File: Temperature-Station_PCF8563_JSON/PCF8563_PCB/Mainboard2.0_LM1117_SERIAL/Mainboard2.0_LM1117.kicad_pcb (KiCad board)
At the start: 2 copper layers, 32 parts, among them J1 CONN_01X03, J2 CONN_01X03, J4 SD_Card, J5 CONN_01X03, J6 CONN_01X02, J7 CONN_01X02, SW1 RESET, SW2 FLASH, U1 LM1117-3.3, U2 PCF8563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

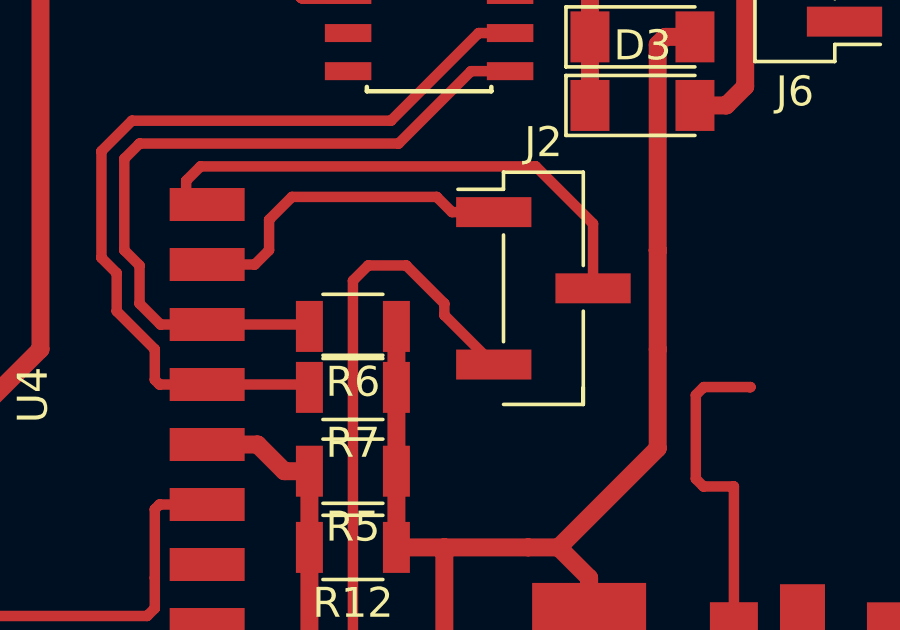
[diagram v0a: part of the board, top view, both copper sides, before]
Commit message: Updates
Updated both versions
Added online updater
Minor cosmetic changes
Saving DHCP settings restored
Added authentication (still no HTTPS/TLS/SSL tho)
Moved as many Strings as possible to Flash memory to free RAM

Czas library:
Optimized for porting between DS3231 and PCF8563 versions.
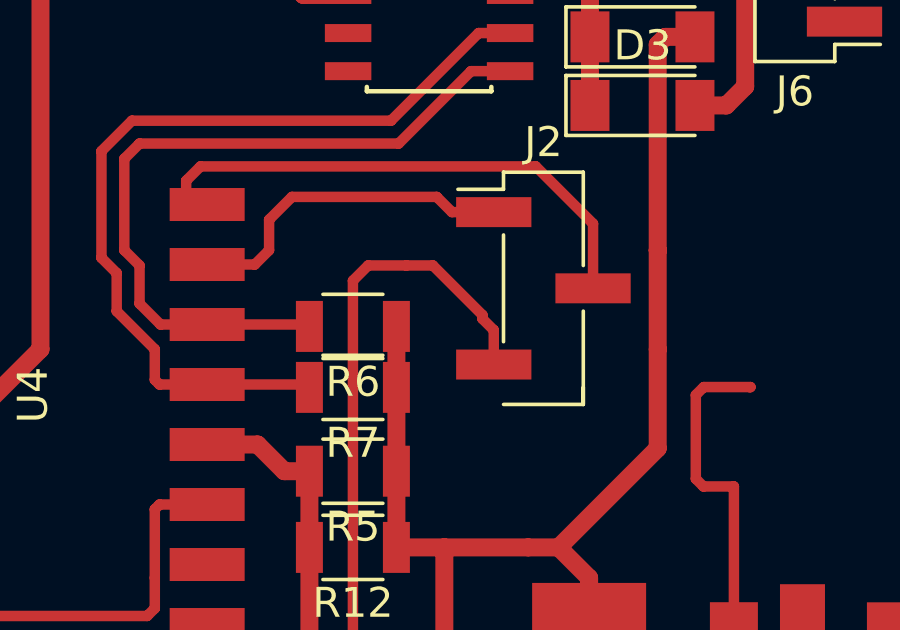
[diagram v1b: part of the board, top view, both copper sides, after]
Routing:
- net GND: track 95.2 -> 95.8 mm
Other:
- net class Default: trace_width 0.35 -> 0.25
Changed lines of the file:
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@@
-(kicad_pcb (version 4) (host pcbnew 4.0.6)
+(kicad_pcb (version 20170919) (host pcbnew "(2017-09-19 revision dddaa7e69)-makepkg")
   (general
-    (links 71)
-    (no_connects 2)
-    (area 0 0 0 0)
     (thickness 1.6)
     (drawings 0)
-    (tracks 276)
+    (tracks 278)
     (zones 0)
     (modules 32)
@@
   (layers
     (0 F.Cu signal)
-    (31 B.Cu signal hide)
-    (32 B.Adhes user hide)
-    (33 F.Adhes user hide)
-    (34 B.Paste user hide)
+    (31 B.Cu signal)
+    (32 B.Adhes user)
+    (33 F.Adhes user)
+    (34 B.Paste user)
     (35 F.Paste user)
-    (36 B.SilkS user hide)
+    (36 B.SilkS user)
     (37 F.SilkS user)
-    (38 B.Mask user hide)
+    (38 B.Mask user)
     (39 F.Mask user)
-    (40 Dwgs.User user hide)
-    (41 Cmts.User user hide)
-    (42 Eco1.User user hide)
-    (43 Eco2.User user hide)
-    (44 Edge.Cuts user hide)
-    (45 Margin user hide)
-    (46 B.CrtYd user hide)
+    (40 Dwgs.User user)
+    (41 Cmts.User user)
+    (42 Eco1.User user)
+    (43 Eco2.User user)
+    (44 Edge.Cuts user)
+    (45 Margin user)
+    (46 B.CrtYd user)
     (47 F.CrtYd user)
-    (48 B.Fab user hide)
+    (48 B.Fab user)
     (49 F.Fab user)
   )
   (setup
-    (last_trace_width 0.35)
+    (last_trace_width 0.25)
     (trace_clearance 0.2)
     (zone_clearance 0.5)
@@
     (pad_to_mask_clearance 0)
     (aux_axis_origin 0 0)
-    (visible_elements 7FFC7A21)
+    (visible_elements 7FFFFE7F)
     (pcbplotparams
       (layerselection 0x00000_00000001)
       (usegerberextensions false)
+      (usegerberattributes true)
+      (usegerberadvancedattributes true)
+      (creategerberjobfile true)
       (excludeedgelayer true)
       (linewidth 0.050000)
@@
       (hpglpenspeed 20)
       (hpglpendiameter 15)
-      (hpglpenoverlay 2)
       (psnegative false)
       (psa4output false)
@@
   (net_class Default "To jest domyślna klasa połączeń."
     (clearance 0.2)
-    (trace_width 0.35)
+    (trace_width 0.25)
     (via_dia 0.6)
     (via_drill 0.4)
@@
     (fp_line (start 3.45 4.35) (end 3.45 -4.35) (layer F.CrtYd) (width 0.05))
     (fp_line (start 3.45 -4.35) (end -3.45 -4.35) (layer F.CrtYd) (width 0.05))
-    (fp_text user %R (at -4.318 4.064 360) (layer F.Fab)
+    (fp_text user %R (at -4.318 4.064) (layer F.Fab)
       (effects (font (size 1 1) (thickness 0.15)))
     )
@@
     (fp_line (start 3.45 4.35) (end 3.45 -4.35) (layer F.CrtYd) (width 0.05))
     (fp_line (start 3.45 -4.35) (end -3.45 -4.35) (layer F.CrtYd) (width 0.05))
-    (fp_text user %R (at 0 4.572 360) (layer F.Fab)
+    (fp_text user %R (at 0 4.572) (layer F.Fab)
       (effects (font (size 1 1) (thickness 0.15)))
     )
@@
   )
   (segment (start 95.01 95.098) (end 97.384 95.098) (width 0.6) (layer F.Cu) (net 1))
+  (segment (start 95.366 94.742) (end 95.01 95.098) (width 0.6) (layer F.Cu) (net 1))
+  (segment (start 97.384 95.098) (end 97.536 94.946) (width 0.6) (layer F.Cu) (net 1))
   (segment (start 97.536 94.946) (end 97.536 93.44) (width 0.6) (layer F.Cu) (net 1))
-  (segment (start 97.384 95.098) (end 97.536 94.946) (width 0.6) (layer F.Cu) (net 1))
   (segment (start 97.536 93.44) (end 99.822 93.44) (width 0.6) (layer F.Cu) (net 1))
   (segment (start 102.87 93.694) (end 100.076 93.694) (width 0.6) (layer F.Cu) (net 1))
   (segment (start 100.076 93.694) (end 99.822 93.44) (width 0.6) (layer F.Cu) (net 1))
-  (segment (start 95.366 94.742) (end 95.01 95.098) (width 0.6) (layer F.Cu) (net 1))
-  (segment (start 87.884 78.486) (end 87.884 78.871) (width 0.35) (layer F.Cu) (net 2))
-  (segment (start 87.884 78.486) (end 86.614 77.216) (width 0.35) (layer F.Cu) (net 2))
-  (segment (start 86.614 77.216) (end 85.344 77.216) (width 0.35) (layer F.Cu) (net 2))
-  (segment (start 85.344 77.216) (end 84.836 77.724) (width 0.35) (layer F.Cu) (net 2))
-  (segment (start 84.836 77.724) (end 84.836 93.98) (width 0.35) (layer F.Cu) (net 2))
-  (segment (start 84.836 93.98) (end 81.28 97.536) (width 0.35) (layer F.Cu) (net 2))
-  (segment (start 81.28 97.536) (end 74.676 97.536) (width 0.35) (layer F.Cu) (net 2))
-  (segment (start 74.676 97.536) (end 73.406 98.806) (width 0.35) (layer F.Cu) (net 2))
-  (segment (start 73.406 98.806) (end 61.722 98.806) (width 0.35) (layer F.Cu) (net 2))
-  (segment (start 61.722 98.806) (end 58.346 95.43) (width 0.35) (layer F.Cu) (net 2))
-  (segment (start 58.346 91.694) (end 58.346 95.43) (width 0.35) (layer F.Cu) (net 2))
-  (segment (start 87.884 78.871) (end 89.531 80.518) (width 0.35) (layer F.Cu) (net 2) (status 800000))
-  (segment (start 97.536 84.582) (end 96.52 84.582) (width 0.35) (layer F.Cu) (net 2))
-  (segment (start 97.536 89.44) (end 97.536 84.582) (width 0.35) (layer F.Cu) (net 2))
+  (segment (start 89.531 79.371) (end 89.531 80.518) (width 0.35) (layer F.Cu) (net 2))
+  (segment (start 89.154 78.994) (end 89.531 79.371) (width 0.35) (layer F.Cu) (net 2))
+  (segment (start 89.154 78.867) (end 89.154 78.994) (width 0.35) (layer F.Cu) (net 2))
+  (segment (start 87.503 77.216) (end 89.154 78.867) (width 0.35) (layer F.Cu) (net 2))
+  (segment (start 86.614 77.216) (end 87.503 77.216) (width 0.35) (layer F.Cu) (net 2))
   (segment (start 96.531 81.269) (end 98.088 81.269) (width 0.35) (layer F.Cu) (net 2))
   (segment (start 96.266 81.534) (end 96.531 81.269) (width 0.35) (layer F.Cu) (net 2))
   (segment (start 96.266 84.328) (end 96.266 81.534) (width 0.35) (layer F.Cu) (net 2))
   (segment (start 96.52 84.582) (end 96.266 84.328) (width 0.35) (layer F.Cu) (net 2))
+  (segment (start 98.077 81.28) (end 98.088 81.269) (width 0.35) (layer F.Cu) (net 2))
+  (segment (start 97.536 84.582) (end 96.52 84.582) (width 0.35) (layer F.Cu) (net 2))
+  (segment (start 97.536 89.44) (end 97.536 84.582) (width 0.35) (layer F.Cu) (net 2))
   (segment (start 97.028 88.932) (end 97.536 89.44) (width 0.35) (layer F.Cu) (net 2))
-  (segment (start 98.077 81.28) (end 98.088 81.269) (width 0.35) (layer F.Cu) (net 2))
+  (segment (start 58.346 91.694) (end 58.346 95.43) (width 0.35) (layer F.Cu) (net 2))
+  (segment (start 61.722 98.806) (end 58.346 95.43) (width 0.35) (layer F.Cu) (net 2))
+  (segment (start 73.406 98.806) (end 61.722 98.806) (width 0.35) (layer F.Cu) (net 2))
+  (segment (start 74.676 97.536) (end 73.406 98.806) (width 0.35) (layer F.Cu) (net 2))
+  (segment (start 81.28 97.536) (end 74.676 97.536) (width 0.35) (layer F.Cu) (net 2))
+  (segment (start 84.836 93.98) (end 81.28 97.536) (width 0.35) (layer F.Cu) (net 2))
+  (segment (start 84.836 77.724) (end 84.836 93.98) (width 0.35) (layer F.Cu) (net 2))
+  (segment (start 85.344 77.216) (end 84.836 77.724) (width 0.35) (layer F.Cu) (net 2))
+  (segment (start 86.614 77.216) (end 85.344 77.216) (width 0.35) (layer F.Cu) (net 2))
   (segment (start 88.424 97.79) (end 88.424 95.218) (width 0.35) (layer F.Cu) (net 2))
   (segment (start 88.544 95.098) (end 90.41 95.098) (width 0.35) (layer F.Cu) (net 2))
@@
   (segment (start 92.583 66.929) (end 92.738 67.084) (width 0.6) (layer F.Cu) (net 4))
   (segment (start 92.738 69.596) (end 92.738 71.882) (width 0.6) (layer F.Cu) (net 4))
-  (segment (start 101.092 97.405) (end 104.017 97.405) (width 0.6) (layer F.Cu) (net 5))
   (segment (start 104.934 89.694) (end 102.87 89.694) (width 0.6) (layer F.Cu) (net 5))
   (segment (start 105.156 89.916) (end 104.934 89.694) (width 0.6) (layer F.Cu) (net 5))
   (segment (start 105.156 96.266) (end 105.156 89.916) (width 0.6) (layer F.Cu) (net 5))
   (segment (start 104.017 97.405) (end 105.156 96.266) (width 0.6) (layer F.Cu) (net 5))
+  (segment (start 101.092 97.405) (end 104.017 97.405) (width 0.6) (layer F.Cu) (net 5))
   (segment (start 97.913 66.548) (end 97.913 71.251) (width 0.6) (layer F.Cu) (net 6))
   (segment (start 97.282 71.882) (end 96.238 71.882) (width 0.6) (layer F.Cu) (net 6))
@@
   (segment (start 83.058 68.072) (end 83.058 65.024) (width 0.6) (layer F.Cu) (net 17))
   (segment (start 83.185 68.199) (end 83.058 68.072) (width 0.6) (layer F.Cu) (net 17))
-  (segment (start 79.278 77.184) (end 81.566 77.184) (width 0.35) (layer F.Cu) (net 18) (status 400000))
-  (segment (start 88.138 75.438) (end 89.531 75.438) (width 0.35) (layer F.Cu) (net 18) (status 800000))
+  (segment (start 79.278 77.184) (end 81.566 77.184) (width 0.35) (layer F.Cu) (net 18))
+  (segment (start 88.138 75.438) (end 89.531 75.438) (width 0.35) (layer F.Cu) (net 18))
   (segment (start 87.63 74.93) (end 88.138 75.438) (width 0.35) (layer F.Cu) (net 18))
   (segment (start 82.804 74.93) (end 87.63 74.93) (width 0.35) (layer F.Cu) (net 18))
@@
   (segment (start 82.042 76.708) (end 82.042 75.692) (width 0.35) (layer F.Cu) (net 18))
   (segment (start 81.566 77.184) (end 82.042 76.708) (width 0.35) (layer F.Cu) (net 18))
-  (segment (start 89.531 75.438) (end 88.646 75.438) (width 0.35) (layer F.Cu) (net 18) (status C00000))
-  (segment (start 92.841 77.978) (end 92.841 75.823) (width 0.35) (layer F.Cu) (net 19) (status 400000))
-  (segment (start 79.278 74.392) (end 79.278 75.184) (width 0.35) (layer F.Cu) (net 19) (status 800000))
+  (segment (start 89.531 75.438) (end 88.646 75.438) (width 0.35) (layer F.Cu) (net 18))
+  (segment (start 92.841 77.978) (end 92.841 75.823) (width 0.35) (layer F.Cu) (net 19))
+  (segment (start 79.278 74.392) (end 79.278 75.184) (width 0.35) (layer F.Cu) (net 19))
   (segment (start 79.756 73.914) (end 79.278 74.392) (width 0.35) (layer F.Cu) (net 19))
   (segment (start 90.932 73.914) (end 79.756 73.914) (width 0.35) (layer F.Cu) (net 19))
   (segment (start 92.841 75.823) (end 90.932 73.914) (width 0.35) (layer F.Cu) (net 19))
-  (segment (start 92.71 77.847) (end 92.841 77.978) (width 0.35) (layer F.Cu) (net 19) (status C00000))
+  (segment (start 92.71 77.847) (end 92.841 77.978) (width 0.35) (layer F.Cu) (net 19))
   (segment (start 61.976 71.374) (end 61.976 73.152) (width 0.6) (layer F.Cu) (net 20))
   (segment (start 58.6 70.792) (end 59.69 71.882) (width 0.6) (layer F.Cu) (net 20))
